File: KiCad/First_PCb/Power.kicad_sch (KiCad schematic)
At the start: 9 parts, among them J5 DC-005, U1 MT3608 TYPE-C USB, U4 EGBO UPS

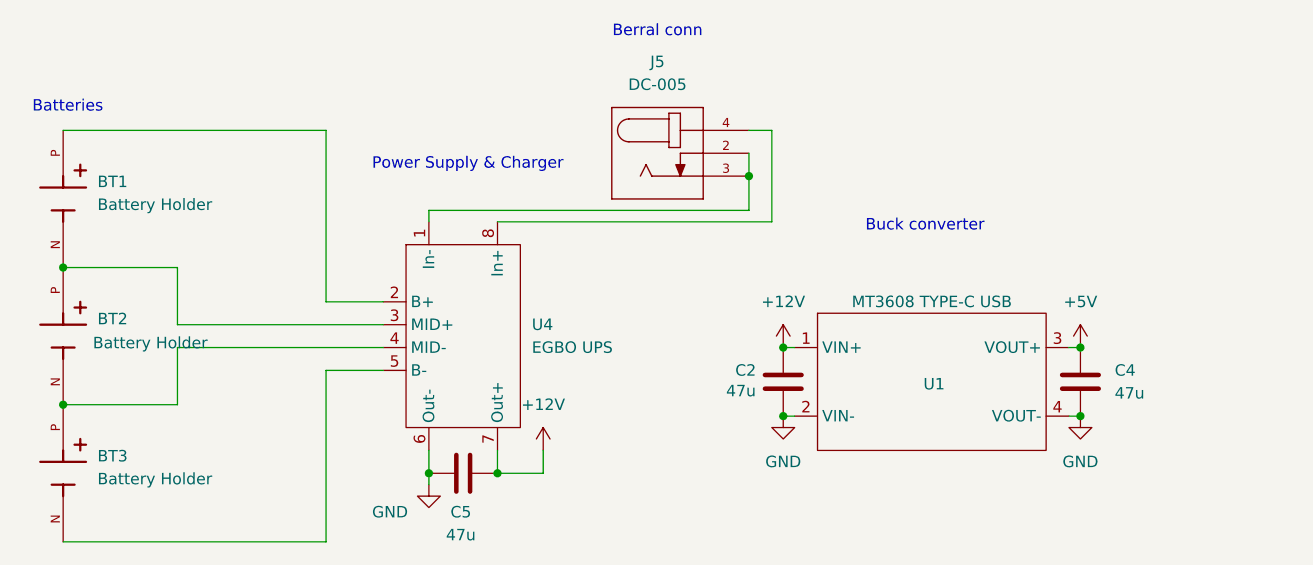
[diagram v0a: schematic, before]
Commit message: added all the kicad files & gerbers of the first pcb
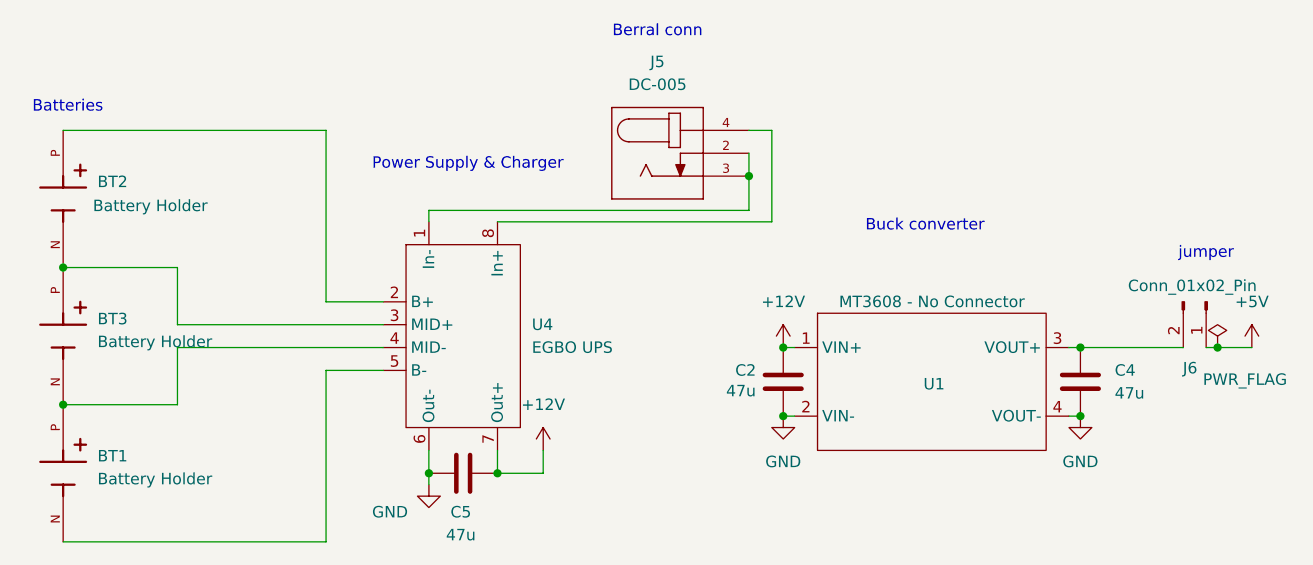
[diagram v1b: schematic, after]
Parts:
- added J6: Conn_01x02_Pin, Connector_PinHeader_2.54mm:PinHeader_1x02_P2.54mm_Vertical, symbol Connector:Conn_01x02_Pin
- U1: value MT3608 TYPE-C USB -> MT3608 - No Connector; footprint footprints:MT3608 Type-C USB -> footprints:MT3608_no_conn_TH
- U4: footprint footprints:PWR_SPLY12V -> footprints:PWR_SPLY12V_TH
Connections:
- net +5V: now also J6.1 (Pin_1); no longer C4.1, U1.3 (VOUT+)
- net at U4.2 (B+): now also BT2.P; no longer BT1.P
- net at BT2.N, BT3.P: now also U4.3 (MID+); no longer U4.4 (MID-)
- net at BT3.N: now also BT1.P, U4.4 (MID-); no longer U4.5 (B-)
- new net: C4.1, J6.2 (Pin_2), U1.3 (VOUT+)
- new net: BT1.N, U4.5 (B-)
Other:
- note added: "jumper"
- moved on the sheet: BT1, BT2, BT3
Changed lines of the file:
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@@
+		)
+	)
+	(text "jumper\n"
+		(exclude_from_sim no)
+		(at 215.9 73.406 0)
+		(effects
+			(font
+				(size 1.27 1.27)
+			)
 		)
 	)
@@
 	)
 	(junction
+		(at 217.17 83.82)
+		(diameter 0)
+		(color 0 0 0 0)
+	)
+	(junction
 		(at 201.93 91.44)
 		(diameter 0)
@@
 	(wire
 		(pts
+			(xy 201.93 83.82) (xy 213.36 83.82)
+		)
+		(stroke
+			(width 0)
+			(type default)
+		)
+	)
+	(wire
+		(pts
 			(xy 101.6 83.82) (xy 124.46 83.82)
 		)
@@
 	(wire
 		(pts
+			(xy 217.17 83.82) (xy 220.98 83.82)
+		)
+		(stroke
+			(width 0)
+			(type default)
+		)
+	)
+	(wire
+		(pts
 			(xy 137.16 97.79) (xy 137.16 95.25)
 		)
@@
 	(wire
 		(pts
+			(xy 215.9 83.82) (xy 217.17 83.82)
+		)
+		(stroke
+			(width 0)
+			(type default)
+		)
+	)
+	(wire
+		(pts
 			(xy 142.24 97.79) (xy 142.24 95.25)
 		)
@@
 			(width 0)
 			(type default)
+		)
+	)
+	(symbol
+		(lib_id "power:PWR_FLAG")
+		(at 217.17 83.82 0)
+		(unit 1)
+		(exclude_from_sim no)
+		(in_bom yes)
+		(on_board yes)
+		(dnp no)
+		(property "Reference" "#FLG02"
+			(at 217.17 81.915 0)
+			(effects
+				(font
+					(size 1.27 1.27)
+				)
+				(hide yes)
+			)
+		)
+		(property "Value" "PWR_FLAG"
+			(at 220.218 87.376 0)
+			(effects
+				(font
+					(size 1.27 1.27)
+				)
+			)
+		)
+		(property "Footprint" ""
+			(at 217.17 83.82 0)
+			(effects
+				(font
+					(size 1.27 1.27)
+				)
+				(hide yes)
+			)
+		)
+		(property "Datasheet" "~"
+			(at 217.17 83.82 0)
+			(effects
+				(font
+					(size 1.27 1.27)
+				)
+				(hide yes)
+			)
+		)
+		(property "Description" "Special symbol for telling ERC where power comes from"
+			(at 217.17 83.82 0)
+			(effects
+				(font
+					(size 1.27 1.27)
+				)
+				(hide yes)
+			)
+		)
+		(pin "1"
+		)
+		(instances
+			(project "first_PCB"
+				(path "/f709486d-613a-44bb-9859-6d5f77e05693/6285590c-ce2a-4b4d-8f7b-9d941974f9a2"
+					(reference "#FLG02")
+					(unit 1)
+				)
+			)
 		)
 	)
@@
 			)
 		)
-		(property "Value" "MT3608 TYPE-C USB"
+		(property "Value" "MT3608 - No Connector"
 			(at 185.42 78.74 0)
 			(effects
@@
 			)
 		)
-		(property "Footprint" "footprints:MT3608 Type-C USB"
+		(property "Footprint" "footprints:MT3608_no_conn_TH"
 			(at 185.42 87.63 0)
 			(effects
@@
 			)
 		)
-		(property "Footprint" "footprints:PWR_SPLY12V"
+		(property "Footprint" "footprints:PWR_SPLY12V_TH"
 			(at 133.35 82.55 0)
 			(effects
@@
 	(symbol
 		(lib_id "spinning_top:Battery Holder")
-		(at 88.9 97.79 270)
+		(at 88.9 82.55 270)
 		(unit 1)
 		(exclude_from_sim no)
@@
 		(fields_autoplaced yes)
 		(property "Reference" "BT3"
-			(at 92.71 95.8849 90)
+			(at 92.71 80.6449 90)
 			(effects
 				(font
@@
 		)
 		(property "Value" "Battery Holder"
-			(at 92.71 98.4249 90)
+			(at 92.71 83.1849 90)
 			(effects
 				(font
@@
 		)
 		(property "Footprint" "footprints:battery_holder"
-			(at 95.25 98.552 0)
+			(at 95.25 83.312 0)
 			(effects
 				(font
@@
 		)
 		(property "Datasheet" ""
-			(at 88.9 97.79 0)
+			(at 88.9 82.55 0)
 			(effects
 				(font
@@
 		)
 		(property "Description" ""
-			(at 88.9 97.79 0)
+			(at 88.9 82.55 0)
 			(effects
 				(font
@@
 		)
 		(instances
-			(project "Smart_Spinner"
+			(project "first_PCB"
 				(path "/f709486d-613a-44bb-9859-6d5f77e05693/6285590c-ce2a-4b4d-8f7b-9d941974f9a2"
 					(reference "BT3")
@@
 	)
 	(symbol
+		(lib_id "Connector:Conn_01x02_Pin")
+		(at 215.9 78.74 270)
+		(unit 1)
+		(exclude_from_sim no)
+		(in_bom yes)
+		(on_board yes)
+		(dnp no)
+		(property "Reference" "J6"
+			(at 214.122 86.106 90)
+			(effects
+				(font
+					(size 1.27 1.27)
+				)
+			)
+		)
+		(property "Value" "Conn_01x02_Pin"
+			(at 214.376 76.962 90)
+			(effects
+				(font
+					(size 1.27 1.27)
+				)
+			)
+		)
+		(property "Footprint" "Connector_PinHeader_2.54mm:PinHeader_1x02_P2.54mm_Vertical"
+			(at 215.9 78.74 0)
+			(effects
+				(font
+					(size 1.27 1.27)
+				)
+				(hide yes)
+			)
+		)
+		(property "Datasheet" "~"
+			(at 215.9 78.74 0)
+			(effects
+				(font
+					(size 1.27 1.27)
+				)
+				(hide yes)
+			)
+		)
+		(property "Description" "Generic connector, single row, 01x02, script generated"
+			(at 215.9 78.74 0)
+			(effects
+				(font
+					(size 1.27 1.27)
+				)
+				(hide yes)
+			)
+		)
+		(pin "2"
+		)
+		(pin "1"
+		)
+		(instances
+			(project "first_PCB"
+				(path "/f709486d-613a-44bb-9859-6d5f77e05693/6285590c-ce2a-4b4d-8f7b-9d941974f9a2"
+					(reference "J6")
+					(unit 1)
+				)
+			)
+		)
+	)
+	(symbol
 		(lib_id "power:+12V")
-		(at 201.93 83.82 0)
+		(at 220.98 83.82 0)
 		(unit 1)
 		(exclude_from_sim no)
@@
 		(fields_autoplaced yes)
 		(property "Reference" "#PWR04"
-			(at 201.93 87.63 0)
+			(at 220.98 87.63 0)
 			(effects
 				(font
@@
 		)
 		(property "Value" "+5V"
-			(at 201.93 78.74 0)
+			(at 220.98 78.74 0)
 			(effects
 				(font
@@
 		)
 		(property "Footprint" ""
-			(at 201.93 83.82 0)
+			(at 220.98 83.82 0)
 			(effects
 				(font
@@
 		)
 		(property "Datasheet" ""
-			(at 201.93 83.82 0)
+			(at 220.98 83.82 0)
 			(effects
 				(font
@@
 		)
 		(property "Description" "Power symbol creates a global label with name \"+12V\""
-			(at 201.93 83.82 0)
+			(at 220.98 83.82 0)
 			(effects
 				(font
@@
 		)
 		(instances
-			(project "Smart_Spinner"
+			(project "first_PCB"
 				(path "/f709486d-613a-44bb-9859-6d5f77e05693/6285590c-ce2a-4b4d-8f7b-9d941974f9a2"
 					(reference "#PWR04")
@@
 		(lib_name "Battery Holder_2")
 		(lib_id "spinning_top:Battery Holder")
-		(at 88.9 82.55 270)
+		(at 88.9 67.31 270)
 		(unit 1)
 		(exclude_from_sim no)
@@
 		(dnp no)
 		(property "Reference" "BT2"
-			(at 92.71 80.6449 90)
+			(at 92.71 65.4049 90)
 			(effects
 				(font
@@
 		)
 		(property "Value" "Battery Holder"
-			(at 92.202 83.312 90)
+			(at 92.202 68.072 90)
 			(effects
 				(font
@@
 		)
 		(property "Footprint" "footprints:battery_holder"
-			(at 95.25 83.312 0)
+			(at 95.25 68.072 0)
 			(effects
 				(font
@@
 		)
 		(property "Datasheet" ""
-			(at 88.9 82.55 0)
+			(at 88.9 67.31 0)
 			(effects
 				(font
@@
 		)
 		(property "Description" ""
-			(at 88.9 82.55 0)
+			(at 88.9 67.31 0)
 			(effects
 				(font
@@
 		)
 		(instances
-			(project "Smart_Spinner"
+			(project "first_PCB"
 				(path "/f709486d-613a-44bb-9859-6d5f77e05693/6285590c-ce2a-4b4d-8f7b-9d941974f9a2"
 					(reference "BT2")
@@
 		(lib_name "Battery Holder_1")
 		(lib_id "spinning_top:Battery Holder")
-		(at 88.9 67.31 270)
+		(at 88.9 97.79 270)
 		(unit 1)
 		(exclude_from_sim no)
@@
 		(fields_autoplaced yes)
 		(property "Reference" "BT1"
-			(at 92.71 65.4049 90)
+			(at 92.71 95.8849 90)
 			(effects
 				(font
@@
 		)
 		(property "Value" "Battery Holder"
-			(at 92.71 67.9449 90)
+			(at 92.71 98.4249 90)
 			(effects
 				(font
@@
 		)
 		(property "Footprint" "footprints:battery_holder"
-			(at 83.82 67.818 0)
+			(at 83.82 98.298 0)
 			(effects
 				(font
@@
 		)
 		(property "Datasheet" ""
-			(at 88.9 67.31 0)
+			(at 88.9 97.79 0)
 			(effects
 				(font
@@
 		)
 		(property "Description" ""
-			(at 88.9 67.31 0)
+			(at 88.9 97.79 0)
 			(effects
 				(font
@@
 		)
 		(instances
-			(project "Smart_Spinner"
+			(project "first_PCB"
 				(path "/f709486d-613a-44bb-9859-6d5f77e05693/6285590c-ce2a-4b4d-8f7b-9d941974f9a2"
 					(reference "BT1")
